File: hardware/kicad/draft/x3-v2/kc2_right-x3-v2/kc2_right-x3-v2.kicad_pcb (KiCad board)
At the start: 2 copper layers, 164.9 x 127.8 mm, 81 parts, among them SW1 KEY_01, SW10 KEY_10, SW11 KEY_11, SW12 KEY_12, SW13 KEY_13, SW14 KEY_14, SW15 KEY_15, SW16 KEY_16, SW17 KEY_17, SW18 KEY_18, SW19 KEY_19, SW2 KEY_02, SW20 KEY_20, SW21 KEY_21, SW22 KEY_22, SW23 KEY_23, SW24 KEY_24, SW25 KEY_25, SW26 KEY_26, SW27 KEY_27, SW28 KEY_28, SW29 KEY_29, SW3 KEY_03, SW30 KEY_30, SW31 KEY_31, SW32 KEY_32, SW33 KEY_33, SW34 KEY_34, SW35 KEY_35, SW36 KEY_36, SW37 KEY_37, SW38 KEY_38, SW39 KEY_39, SW4 KEY_04, SW5 KEY_05, SW6 KEY_06, SW7 KEY_07, SW8 KEY_08, SW9 KEY_09, U1 nice!nano_v2_socket_24pin

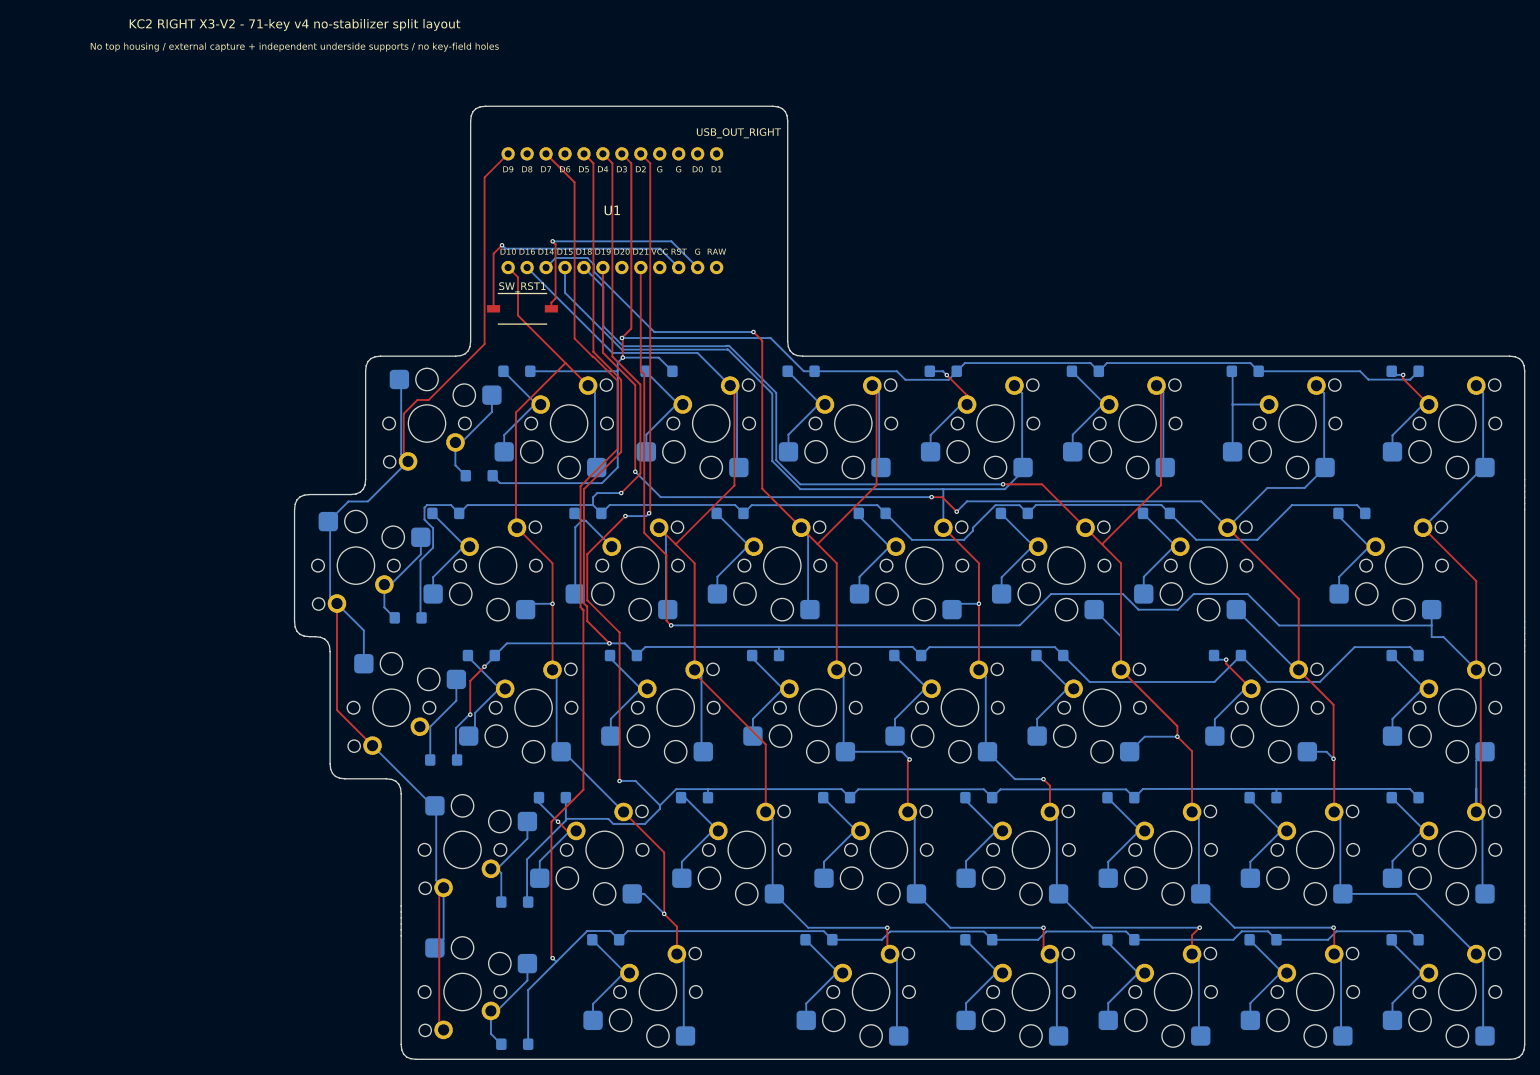
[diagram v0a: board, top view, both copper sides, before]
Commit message: feat(hardware): complete KC2 X3 V2 digital draft
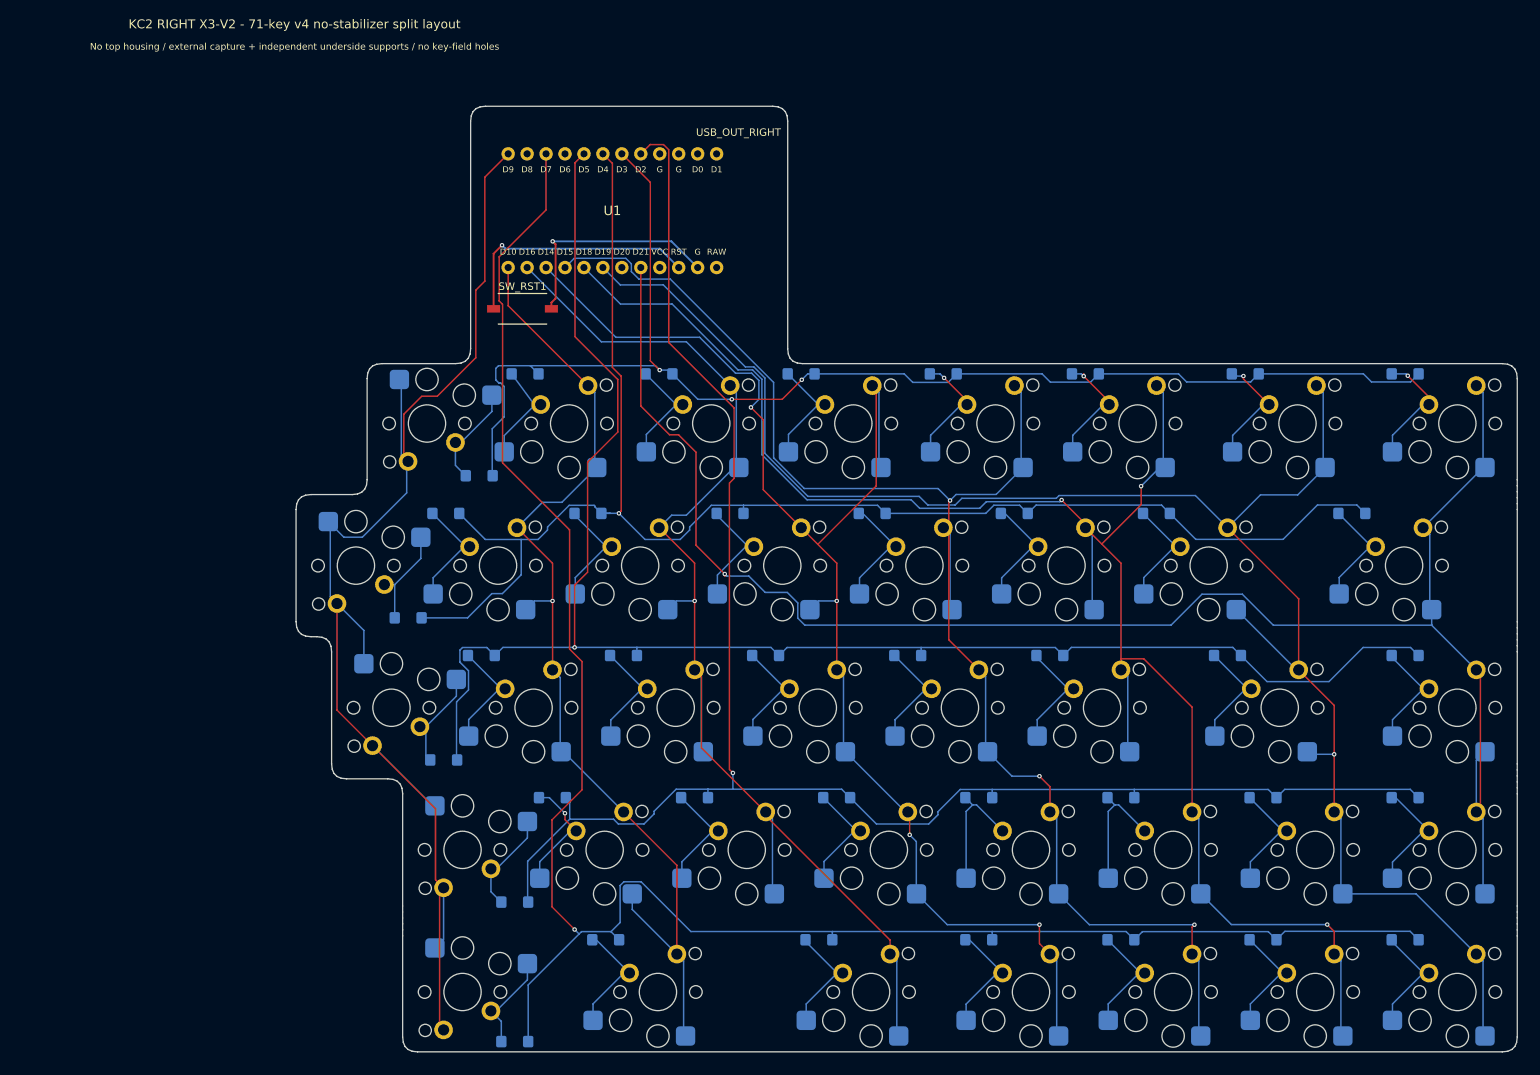
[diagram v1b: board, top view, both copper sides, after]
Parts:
- moved D2 1.15 mm to (65.9, 70.9)
- moved D3 0.35 mm to (83.8, 70.9)
- moved D33 0.35 mm to (64.5, 160.4)
- moved D4 0.35 mm to (102.9, 70.9)
- moved D5 0.35 mm to (122.0, 70.9)
- moved D6 0.35 mm to (141.0, 70.9)
- moved D7 0.35 mm to (162.4, 70.9)
- moved D8 0.35 mm to (183.9, 70.9)
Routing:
- net R_COL7: track 256.3 -> 234.4 mm
- net R_COL3: track 203.9 -> 187.9 mm, vias 3 -> 4
- net R_COL0: track 166.9 -> 182.9 mm
- net R_ROW0: track 193.0 -> 179.1 mm, vias 2 -> 3
- net R_COL2: track 180.6 -> 167.5 mm
- net R_ROW4: track 251.8 -> 259.3 mm
- net R_COL6: track 244.5 -> 237.2 mm, vias 4 -> 1
- net R_COL4: track 196.9 -> 203.9 mm
- net R_COL1: track 143.6 -> 138.0 mm, vias 2 -> 1
- net R_COL5: track 233.3 -> 230.6 mm
- net R_ROW2: track 222.5 -> 225.1 mm, vias 3 -> 1
- net RK11_D: track 17.0 -> 15.0 mm
- net RK29_D: track 15.0 -> 17.0 mm
- net RK30_D: track 15.0 -> 17.0 mm
- net RK06_D: track 15.0 -> 17.0 mm, vias 0 -> 1
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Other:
- board size 164.9 x 127.8 mm -> 163.7 x 126.8 mm

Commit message: fix: add X3 V2 diode edge clearance
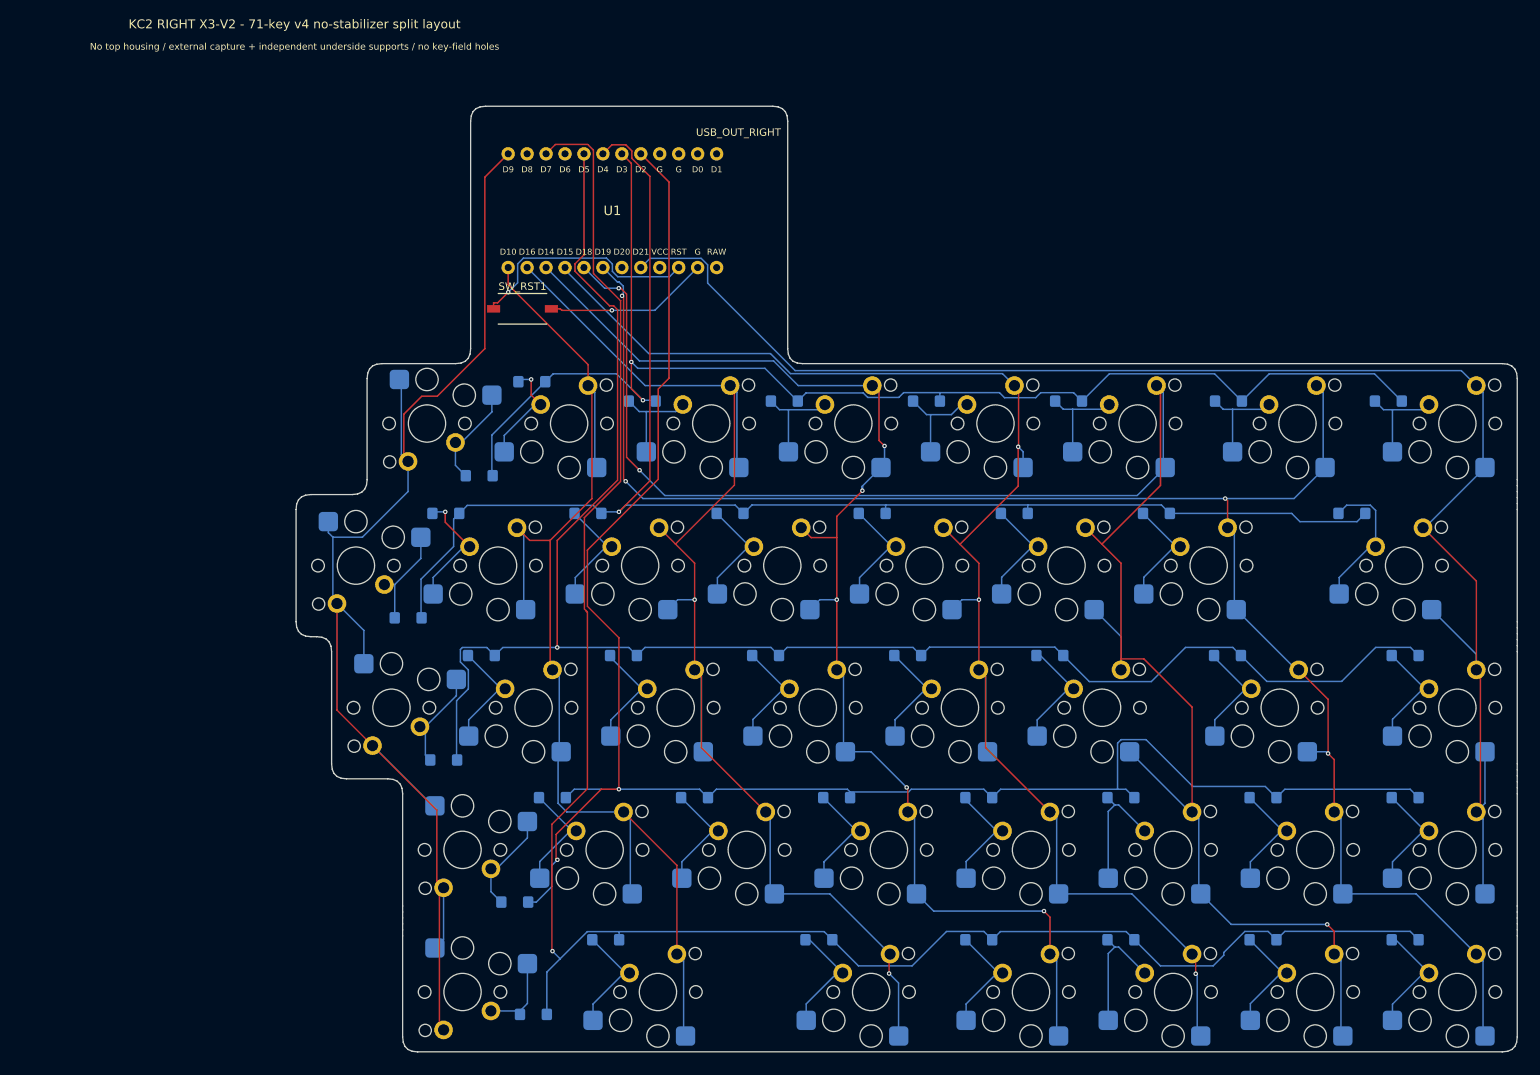
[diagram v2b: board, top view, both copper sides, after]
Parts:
- moved D33 4.42 mm to (67.0, 156.7)
- moved D3 4.29 mm to (81.6, 74.5)
- moved D4 4.29 mm to (100.7, 74.5)
- moved D5 4.29 mm to (119.7, 74.5)
- moved D6 4.29 mm to (138.8, 74.5)
- moved D7 4.29 mm to (160.2, 74.5)
- moved D8 4.29 mm to (181.6, 74.5)
- moved D2 1.38 mm to (66.8, 71.9)
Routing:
- net R_COL5: track 230.6 -> 255.6 mm
- net R_COL1: track 138.0 -> 161.8 mm, vias 1 -> 0
- net R_COL7: track 234.4 -> 216.2 mm, vias 1 -> 0
- net R_COL3: track 187.9 -> 174.5 mm, vias 4 -> 5
- net R_ROW3: track 235.9 -> 246.3 mm, vias 1 -> 2
- net GND: track 30.3 -> 22.1 mm
- net R_ROW1: track 207.3 -> 199.3 mm
- net R_COL4: track 203.9 -> 198.6 mm
- net RK16_D: track 15.0 -> 19.4 mm
- net R_COL2: track 167.5 -> 171.5 mm, vias 1 -> 2
- net R_COL6: track 237.2 -> 233.3 mm, vias 1 -> 4
- net R_ROW2: track 225.1 -> 228.8 mm
- net RK06_D: track 17.0 -> 13.7 mm, vias 1 -> 0
- net RK08_D: track 16.1 -> 13.7 mm, vias 1 -> 0
- net RK33_D: track 13.5 -> 11.1 mm
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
